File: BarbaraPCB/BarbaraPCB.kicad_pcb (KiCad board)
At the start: 2 copper layers, 195.3 x 125.5 mm, 153 parts, among them J1 Conn_01x05_Pin, J2 Conn_01x05_Pin, J3 Conn_01x05_Pin_reversed, J4 Conn_01x05_Pin_reversed, J5 Connector for PAM8403 Amp, SW1 SW_Push, SW10 SW_Push, SW11 SW_Push, SW12 SW_Push, SW13 SW_Push, SW14 SW_Push, SW15 SW_Push, SW16 SW_Push, SW17 SW_Push, SW18 SW_Push, SW19 SW_Push, SW2 SW_Push, SW20 SW_Push, SW21 SW_Push_1.5u, SW22 SW_Push, SW23 SW_Push, SW24 SW_Push, SW25 SW_Push, SW26 SW_Push, SW27 SW_Push, SW28 SW_Push, SW29 SW_Push_1.5u, SW3 SW_Push, SW30 SW_Push, SW31 SW_Push, SW32 SW_Push, SW33 SW_Push, SW34 SW_Push, SW35 SW_Push_1.25u, SW36 SW_Push_1.75u, SW37 SW_Push_1.75u, SW38 SW_Push_1.25u, SW39 SW_Push, SW4 SW_Push, SW40 SW_Push, SW41 SW_Push, SW42 SW_Push, SW43 SW_Push, SW44 SW_Push, SW45 SW_Push_1.5u, SW46 SW_Push_1.5u, SW47 SW_Push_1.5u, SW48 SW_Push_1.5u, SW49 SW_Push, SW5 SW_Push, SW50 SW_Push, SW51 SW_Push, SW52 SW_Push, SW53 SW_Push, SW54 SW_Push_1.25u, SW55 SW_Push_1.75u, SW56 SW_Push_1.75u, SW57 SW_Push_1.25u, SW58 SW_Push, SW59 SW_Push, SW6 SW_Push, SW60 SW_Push, SW61 SW_Push, SW62 SW_Push, SW63 SW_Push, SW64 SW_Push_1.5u, SW65 SW_Push_1.5u, SW66 SW_Push_1.5u, SW67 SW_Push_1.5u, SW7 SW_Push, SW8 SW_Push, SW9 SW_Push, U1 RP2040-Matrix

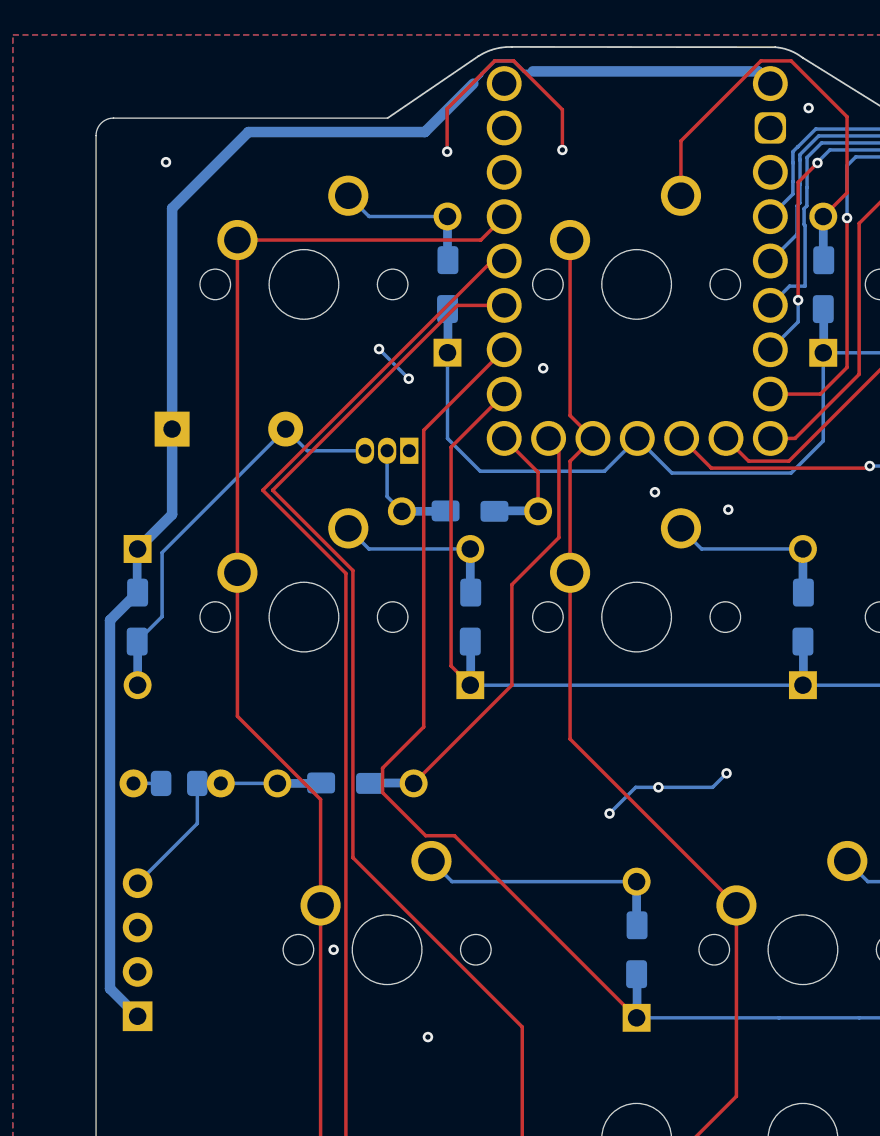
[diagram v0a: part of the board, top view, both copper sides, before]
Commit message: Simplified audio-part. Not amp or transistor needed.
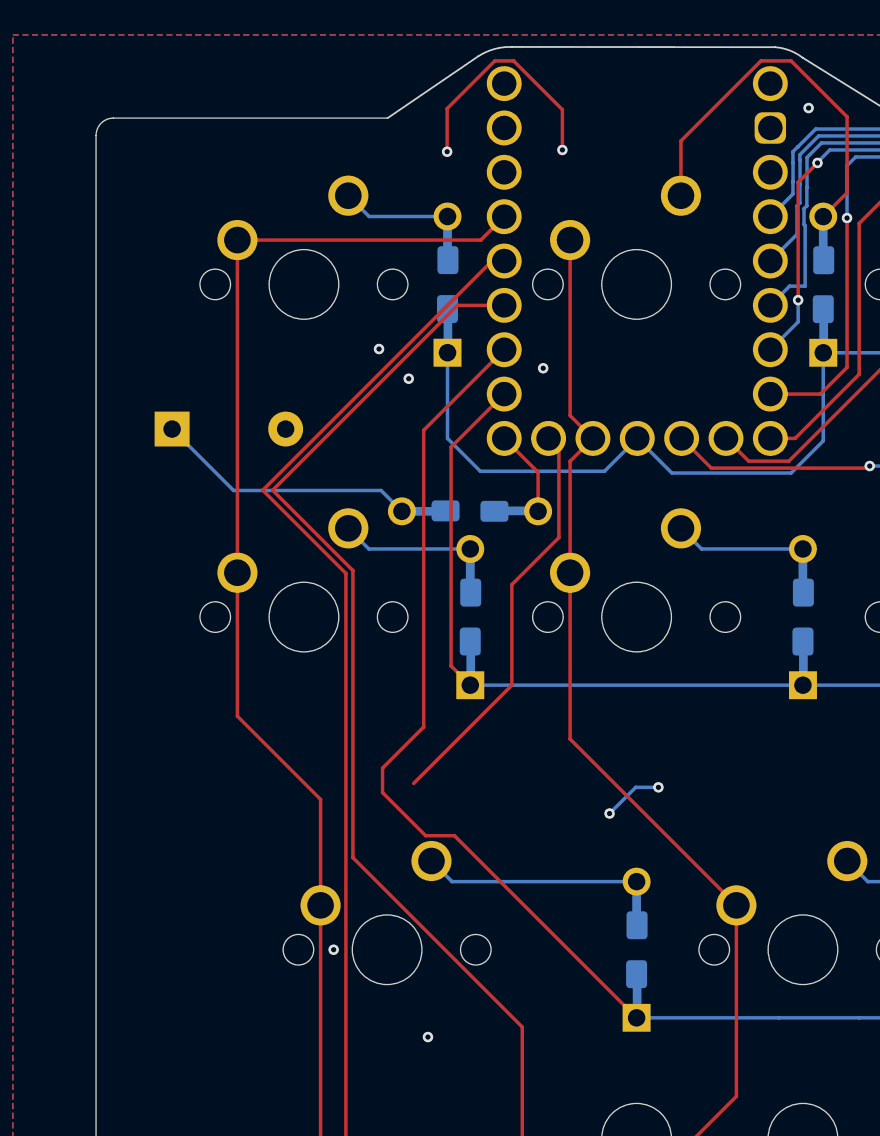
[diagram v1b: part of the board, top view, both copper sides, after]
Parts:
- removed 1k: 1K, TFL:Resistor-dual
- removed C1: 100n, Capacitor_THT:C_Disc_D5.0mm_W2.5mm_P5.00mm
- removed C2: 100n, Capacitor_SMD:C_0805_2012Metric_Pad1.18x1.45mm_HandSolder
- removed D48: 1N4148, TFL:Diode-dual
- removed J5: Connector for PAM8403 Amp, Connector_PinHeader_2.54mm:PinHeader_1x04_P2.54mm_Vertical
- removed PN2222A: PN2222A, Package_TO_SOT_THT:TO-92_Inline
- R1: renamed from 1k; value 1K -> 100
- moved Ref** 5.82 mm to (120.5, 68.3)
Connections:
- BZ1 pad 1: +5V -> Net-(BZ1-+)
- BZ1 pad 2: Net-(BZ1--) -> GND
- R1 pad 2: Net-(Q2-B) -> Net-(BZ1-+)
- U1 pad 23: Net-(U1-P9) -> unconnected-(U1-P9-Pad23)
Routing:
- net +5V: track 84.2 -> 0.00 mm
- net unconnected-(U1-P9-Pad23): track 0.00 -> 23.4 mm
- net Net-(U1-P9): track 23.4 -> 0.00 mm
- net Net-(BZ1--): track 20.7 -> 0.00 mm
- net Net-(BZ1-+): track 0.00 -> 15.1 mm
- net Net-(J5-Pin_4): track 11.7 -> 0.00 mm
- net GND: track 26.2 -> 17.9 mm, vias 31 -> 27
- net Net-(Q2-B): track 3.82 -> 0.00 mm
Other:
- board text added: "100"
- board text added: "Buzzer or Speaker"
- board text added: "Signal (P8)"
- board text removed: "100n"
- board text removed: "5V"
- board text removed: "B"
- board text removed: "C"
- board text removed: "Connector for PAM8403 Amp"
- board text removed: "GND (E)"
- board text removed: "GND(Sig)"
- board text removed: "Reversed!"
- board text removed: "Signal (P9)"
